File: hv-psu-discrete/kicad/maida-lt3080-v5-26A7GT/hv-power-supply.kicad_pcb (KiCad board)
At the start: 2 copper layers, 159.7 x 99.6 mm, 95 parts, among them J1 AC-LV, J10 GND_LV, J11 AC-HV, J12 AC-HV, J13 EARTH, J2 AC-LV, J3 HV, J4 GND_HV, J5 LV, J6 GND_LV, J7 LED, J8 GND_LV, J9 +5V, K1 G6S-2 DC5, Q1 FQPF2N70, Q3 MMBT3904, U1 LT3080xST, U2 LM317_TO-220, U3 LM7805_TO220, U4 TLC555xD

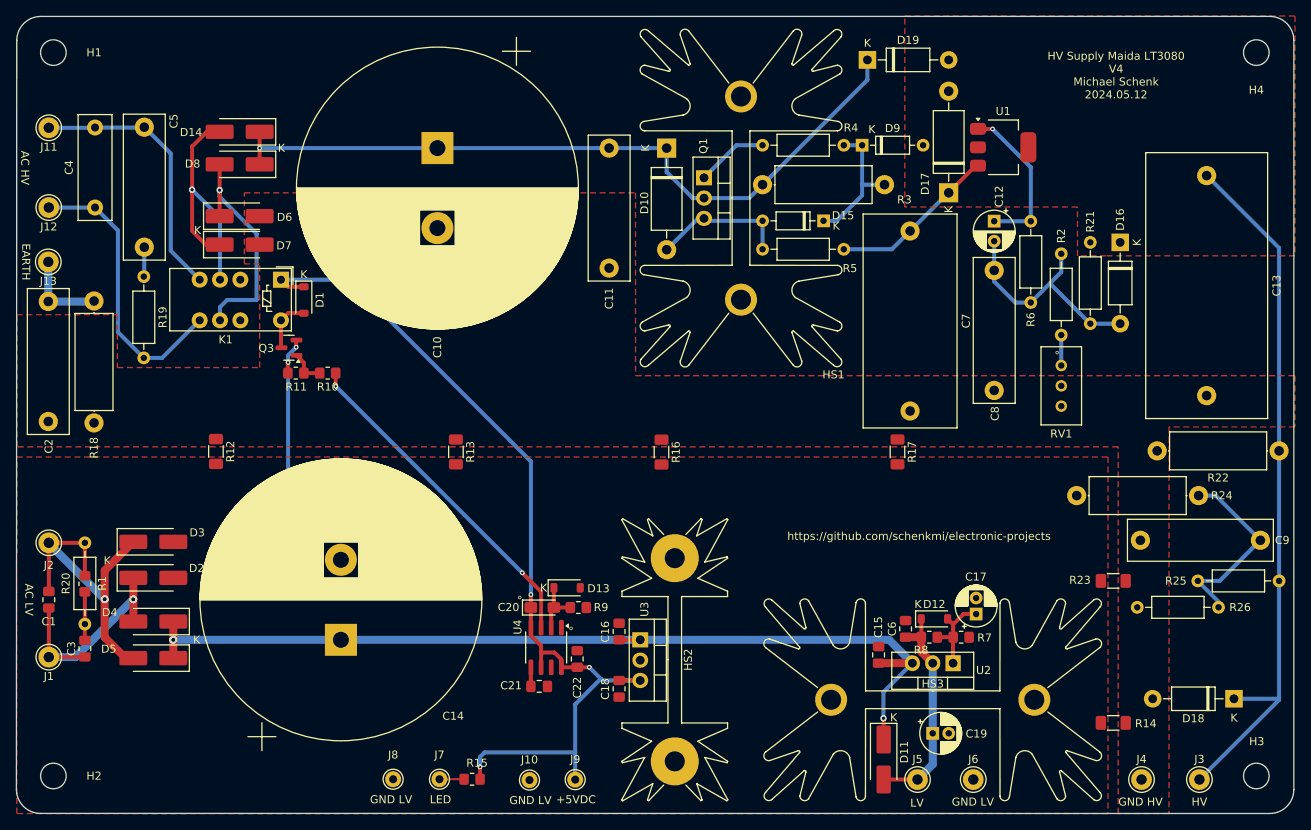
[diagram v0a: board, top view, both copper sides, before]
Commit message: PSU for 26A7 pre amplifier
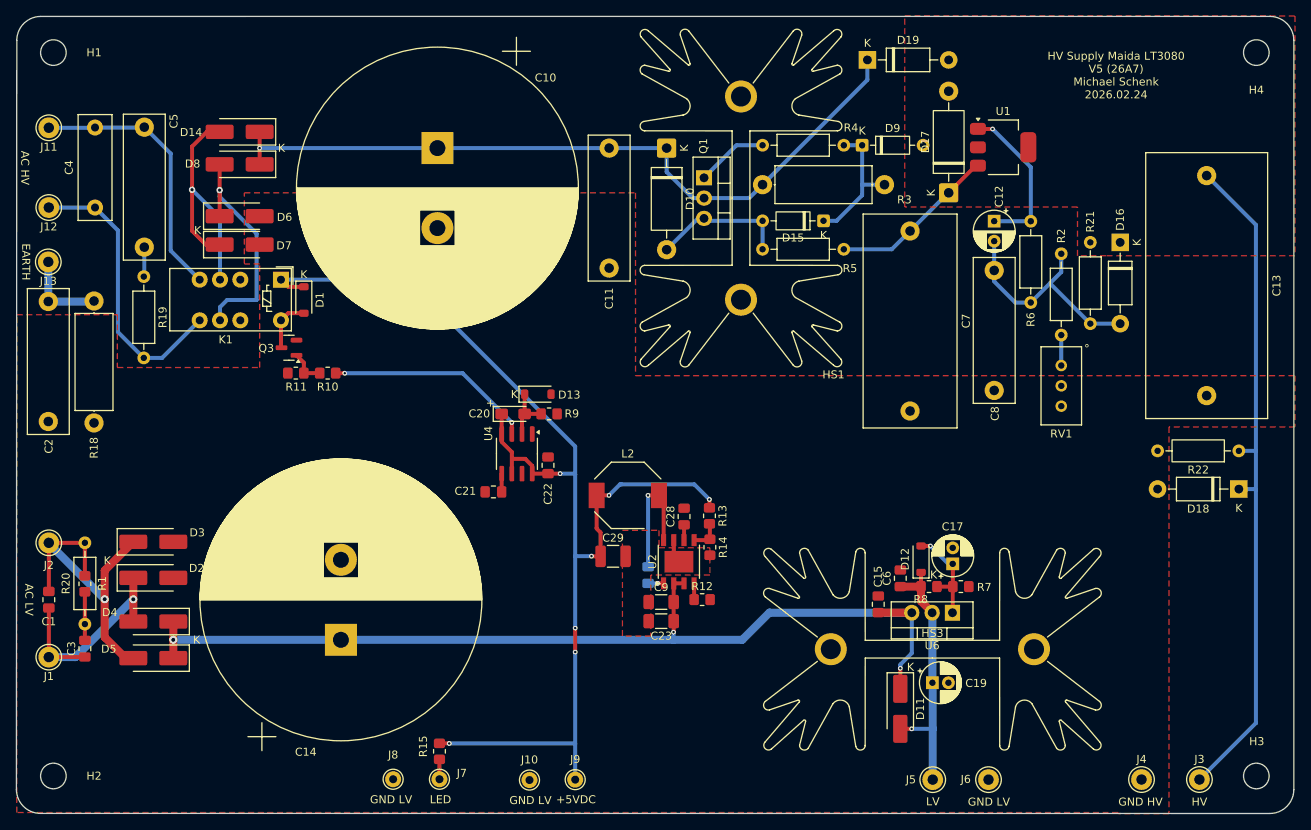
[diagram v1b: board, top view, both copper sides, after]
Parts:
- removed C16: 330nF/50V, Capacitor_SMD:C_0805_2012Metric_Pad1.18x1.45mm_HandSolder
- removed C18: 100nF/50V, Capacitor_SMD:C_0805_2012Metric_Pad1.18x1.45mm_HandSolder
- removed HS2: Heatsink, Heatsink:Heatsink_Fischer_SK104-STC-STIC_35x13mm_2xDrill2.5mm
- removed R16, R17, R23: 0R, Resistor_SMD:R_1206_3216Metric_Pad1.30x1.75mm_HandSolder
- removed R24: 100R/2W, Resistor_THT:R_Axial_DIN0414_L11.9mm_D4.5mm_P15.24mm_Horizontal
- removed R25: 300k/0.6W, Resistor_THT:R_Axial_DIN0207_L6.3mm_D2.5mm_P10.16mm_Horizontal
- removed R26: 100k/0.6W, Resistor_THT:R_Axial_DIN0207_L6.3mm_D2.5mm_P10.16mm_Horizontal
- removed U3: LM7805_TO220, Package_TO_SOT_THT:TO-220-3_Vertical
- added C23: 10uF/50V/X7R, Capacitor_SMD:C_1206_3216Metric_Pad1.33x1.80mm_HandSolder, F.Cu at (130.8, 128.5)
- added C27: 100nF/50V/X7R, Capacitor_SMD:C_0805_2012Metric_Pad1.18x1.45mm_HandSolder, B.Cu at (129.2, 122.7)
- added C28: 10nF/50V, Capacitor_SMD:C_0805_2012Metric_Pad1.18x1.45mm_HandSolder, F.Cu at (133.7, 115.4)
- added C29: 22uF/25V/X7R, Capacitor_SMD:C_1210_3225Metric_Pad1.33x2.70mm_HandSolder, F.Cu at (124.8, 120.4)
- added L2: 15uH, Inductor_SMD:L_Bourns-SRU8028_8.0x8.0mm, F.Cu at (126.7, 112.8)
- added U6: LM350_TO220, Package_TO_SOT_THT:TO-220-3_Vertical, F.Cu at (167.2, 127.4)
- C10: value 680uF/450VDC -> 6800uF/80VDC
- C14: value 22000uF/25VDC -> 10000uF/50V
- C17: value 10uF/25V -> 10uF/50V
- C19: value 1uF/25V -> 1uF/50V
- C9: value 100nF/630V -> 10uF/50V/X7R; footprint Capacitor_THT:C_Rect_L18.0mm_W5.0mm_P15.00mm_FKS3_FKP3 -> Capacitor_SMD:C_1206_3216Metric_Pad1.33x1.80mm_HandSolder
- R12: value 0R -> 200k; footprint Resistor_SMD:R_1206_3216Metric_Pad1.30x1.75mm_HandSolder -> Resistor_SMD:R_0805_2012Metric_Pad1.20x1.40mm_HandSolder
- R13: value 0R -> 52.3k; footprint Resistor_SMD:R_1206_3216Metric_Pad1.30x1.75mm_HandSolder -> Resistor_SMD:R_0805_2012Metric_Pad1.20x1.40mm_HandSolder
- R14: value 0R -> 10k; footprint Resistor_SMD:R_1206_3216Metric_Pad1.30x1.75mm_HandSolder -> Resistor_SMD:R_0805_2012Metric_Pad1.20x1.40mm_HandSolder
- R2: value 0R/180k/0.6W -> 22k/0.6W
- R22: value 100k/2W -> 27k/1W; footprint Resistor_THT:R_Axial_DIN0414_L11.9mm_D4.5mm_P15.24mm_Horizontal -> Resistor_THT:R_Axial_DIN0207_L6.3mm_D2.5mm_P10.16mm_Horizontal
- R7: value 976R -> 4.75k
- RV1: value 50k/500k -> 50k
- U2: value LM317_TO-220 -> AP64102SP-13; footprint Package_TO_SOT_THT:TO-220-3_Vertical -> Package_SO:Diodes_PSOP-8
- moved R12 63.5 mm to (136.0, 125.8), turned to 0 degrees
- moved C9 60.4 mm to (130.8, 126.1)
- moved R14 55.0 mm to (136.9, 119.2), turned to -90 degrees
- moved U2 36.5 mm to (133.1, 121.0), turned to 90 degrees
- moved R13 32.7 mm to (136.9, 115.3)
- moved D18 26.2 mm to (203.0, 112.0)
- moved C21 25.0 mm to (109.9, 112.3)
- moved C22 24.5 mm to (116.7, 109.0)
- moved U4 24.5 mm to (112.8, 107.6)
- moved C20 24.5 mm to (112.3, 102.6)
- moved R9 24.5 mm to (116.8, 102.6)
- moved D13 24.5 mm to (115.4, 100.1)
- moved D12 7.65 mm to (163.3, 120.7), turned to 90 degrees
- moved C17 6.92 mm to (167.3, 121.3)
- moved D11 6.66 mm to (160.7, 139.4)
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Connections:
- C10 pad 2: GND_HV -> GND
- C11 pad 2: GND_HV -> GND
- C13 pad 2: GND_HV -> GND
- C14 pad 2: GND_LV -> GND
- C15 pad 2: GND_LV -> GND
- C17 pad 2: GND_LV -> GND
- C19 pad 2: GND_LV -> GND
- C2 pad 2: GND_HV -> GND
- C21 pad 1: Net-(U4-CV) -> GND
- C21 pad 2: GND_LV -> Net-(U4-CONT)
- C22 pad 2: GND_LV -> GND
- C6 pad 2: GND_LV -> GND
- C7 pad 2: GND_HV -> GND
- C8 pad 2: GND_HV -> GND
- C9 pad 1: GND_HV -> GND
- C9 pad 2: Net-(C9-Pad2) -> Net-(D11-K)
- D13 pad 2: GND_LV -> GND
- D18 pad 2: GND_HV -> GND
- D2 pad 2: GND_LV -> GND
- D3 pad 2: GND_LV -> GND
- D6 pad 2: GND_HV -> GND
- D7 pad 2: GND_HV -> GND
- J10 pad 1: GND_LV -> GND
- J4 pad 1: GND_HV -> GND
- J6 pad 1: GND_LV -> GND
- J8 pad 1: GND_LV -> GND
- Q3 pad 2: GND_LV -> GND
- R11 pad 2: GND_LV -> GND
- R12 pad 1: GND_HV -> Net-(U2-RT/CLK)
- R12 pad 2: GND_LV -> GND
- R13 pad 1: GND_HV -> +5VDC
- R13 pad 2: GND_LV -> Net-(U2-FB)
- R14 pad 1: GND_HV -> Net-(U2-FB)
- R14 pad 2: GND_LV -> GND
- R18 pad 2: GND_HV -> GND
- R22 pad 2: GND_HV -> GND
- R7 pad 2: GND_LV -> GND
- R9 pad 2: GND_LV -> GND
- RV1 pad 2: GND_HV -> GND
- RV1 pad 3: GND_HV -> GND
- U2 pad 1: Net-(D12-A) -> Net-(U2-BST)
- U2 pad 2: Net-(D11-A) -> Net-(D11-K)
- U4 pad 1: GND_LV -> GND
- U4 pad 5: Net-(U4-CV) -> Net-(U4-CONT)
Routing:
- net +5VDC: track 116.0 -> 152.1 mm, vias 3 -> 7
- net Net-(C9-Pad2): track 24.3 -> 0.00 mm
- net GND_LV: track 19.0 -> 0.00 mm, vias 3 -> 0
- net Net-(U4-OUT): track 42.4 -> 26.0 mm
- net Net-(U2-SW): track 0.00 -> 16.1 mm, vias 0 -> 1
- net Net-(D11-A): track 27.7 -> 33.2 mm, vias 0 -> 1
- net Net-(D11-K): track 116.1 -> 121.0 mm, vias 2 -> 3
- net Net-(U2-FB): track 0.00 -> 3.97 mm
- net /HVOUT: track 89.1 -> 85.3 mm
- net GND: track 0.00 -> 2.48 mm
- net Net-(U4-CV): track 2.39 -> 0.00 mm
- net Net-(U4-CONT): track 0.00 -> 2.29 mm
- net Net-(U2-RT/CLK): track 0.00 -> 2.04 mm
- net Net-(U2-BST): track 0.00 -> 1.94 mm, vias 0 -> 1
- net Net-(U2-SS): track 0.00 -> 1.92 mm
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- added copper zone on F.Cu, net GND
- removed copper zone on F.Cu, net GND_HV
- removed copper zone on F.Cu, net GND_LV
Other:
- board text added: "+"
- board text added: "HV Supply Maida LT3080 V5 (26A7) Michael Schenk 2026.02.24"
- board text removed: "HV Supply Maida LT3080 V4 Michael Schenk 2024.05.12"
- board text removed: "https://github.com/schenkmi/electronic-projects"

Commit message: WIP
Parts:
- added G***: LOGO, LOGO, F.Cu at (130.9, 140.0)
- J10, J6, J8: value GND_LV -> GND
- J4: value GND_HV -> GND
- U6: value LM350_TO220 -> LM338
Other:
- board text added: "GND"
- board text removed: "GND HV"
- board text removed: "GND LV"
